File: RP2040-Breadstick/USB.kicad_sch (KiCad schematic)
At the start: 5 parts, among them J601 USB_C_Receptacle_USB2.0

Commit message: More BOM updates
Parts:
- J601: value USB_C_Receptacle_USB2.0 -> (none)
- R601, R602: value 5k1 0603 -> (none); Digikey P123051DKR-ND -> 311-5.10KHRCT-ND; Manufacturer (none) -> YAGEO; Manufacturer_Part_Number (none) -> RC0603FR-075K1L; Mouser (none) -> 603-RC0603FR-075K1L; Package (none) -> 0603
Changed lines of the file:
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@@
       (effects (font (size 1.27 1.27)) (justify left))
     )
-    (property "Value" "5k1 0603" (id 1) (at 128.27 121.92 0)
+    (property "Value" "" (id 1) (at 128.27 121.92 0)
       (effects (font (size 1.27 1.27)) (justify left))
     )
@@
       (effects (font (size 1.27 1.27)) hide)
     )
-    (property "Digikey" "P123051DKR-ND" (id 5) (at 116.84 120.65 0)
+    (property "Digikey" "311-5.10KHRCT-ND" (id 5) (at 116.84 120.65 0)
+      (effects (font (size 1.27 1.27)) hide)
+    )
+    (property "Manufacturer" "YAGEO" (id 6) (at 116.84 120.65 0)
+      (effects (font (size 1.27 1.27)) hide)
+    )
+    (property "Manufacturer_Part_Number" "RC0603FR-075K1L" (id 7) (at 116.84 120.65 0)
+      (effects (font (size 1.27 1.27)) hide)
+    )
+    (property "Mouser" "603-RC0603FR-075K1L" (id 8) (at 116.84 120.65 0)
+      (effects (font (size 1.27 1.27)) hide)
+    )
+    (property "Package" "0603" (id 9) (at 116.84 120.65 0)
       (effects (font (size 1.27 1.27)) hide)
     )
@@
       (effects (font (size 1.27 1.27)) (justify left))
     )
-    (property "Value" "5k1 0603" (id 1) (at 142.24 121.92 0)
+    (property "Value" "" (id 1) (at 142.24 121.92 0)
       (effects (font (size 1.27 1.27)) (justify left))
     )
@@
       (effects (font (size 1.27 1.27)) hide)
     )
-    (property "Digikey" "P123051DKR-ND" (id 5) (at 130.81 120.65 0)
+    (property "Digikey" "311-5.10KHRCT-ND" (id 5) (at 130.81 120.65 0)
+      (effects (font (size 1.27 1.27)) hide)
+    )
+    (property "Manufacturer" "YAGEO" (id 6) (at 130.81 120.65 0)
+      (effects (font (size 1.27 1.27)) hide)
+    )
+    (property "Manufacturer_Part_Number" "RC0603FR-075K1L" (id 7) (at 130.81 120.65 0)
+      (effects (font (size 1.27 1.27)) hide)
+    )
+    (property "Mouser" "603-RC0603FR-075K1L" (id 8) (at 130.81 120.65 0)
+      (effects (font (size 1.27 1.27)) hide)
+    )
+    (property "Package" "0603" (id 9) (at 130.81 120.65 0)
       (effects (font (size 1.27 1.27)) hide)
     )
@@
     (in_bom yes) (on_board yes) (fields_autoplaced)
     (property "Reference" "J601" (id 0) (at 88.9 77.47 0))
-    (property "Value" "USB_C_Receptacle_USB2.0" (id 1) (at 88.9 80.01 0))
+    (property "Value" "" (id 1) (at 88.9 80.01 0))
     (property "Footprint" "" (id 2) (at 92.71 100.33 0)
       (effects (font (size 1.27 1.27)) hide)

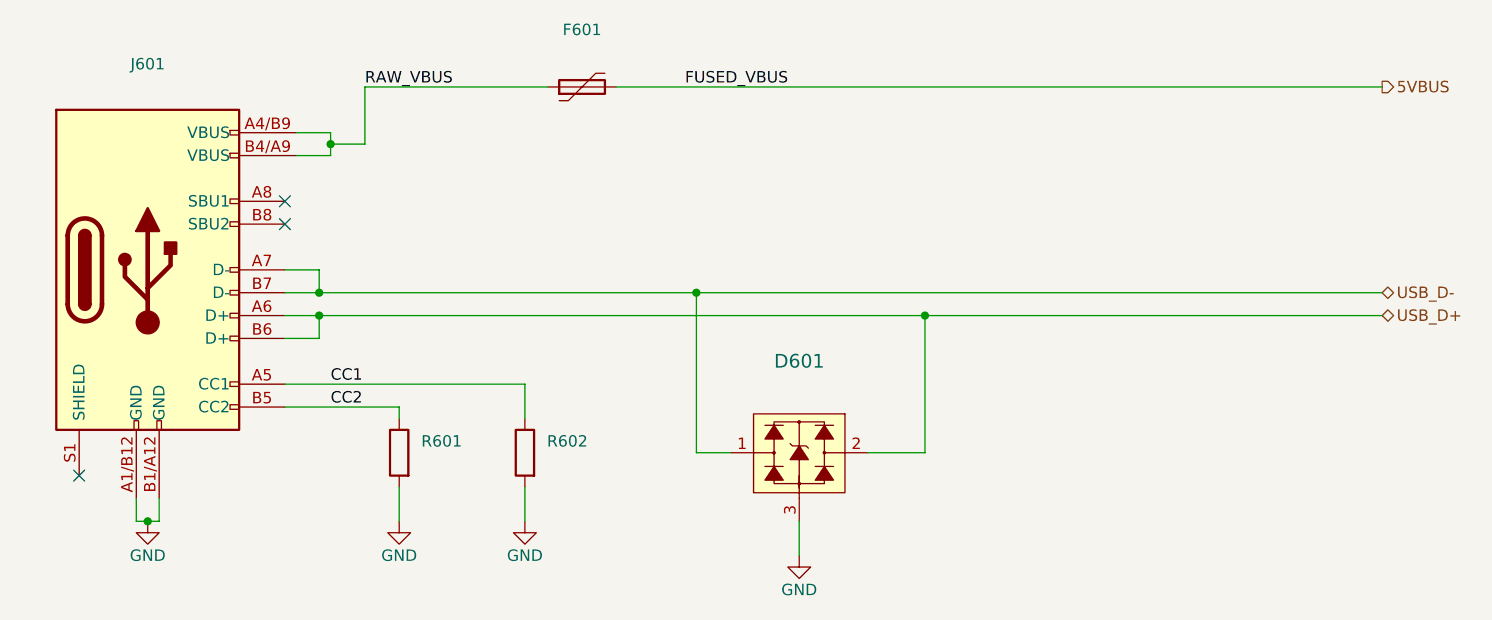
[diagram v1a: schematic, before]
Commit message: Created BOM spreadsheet
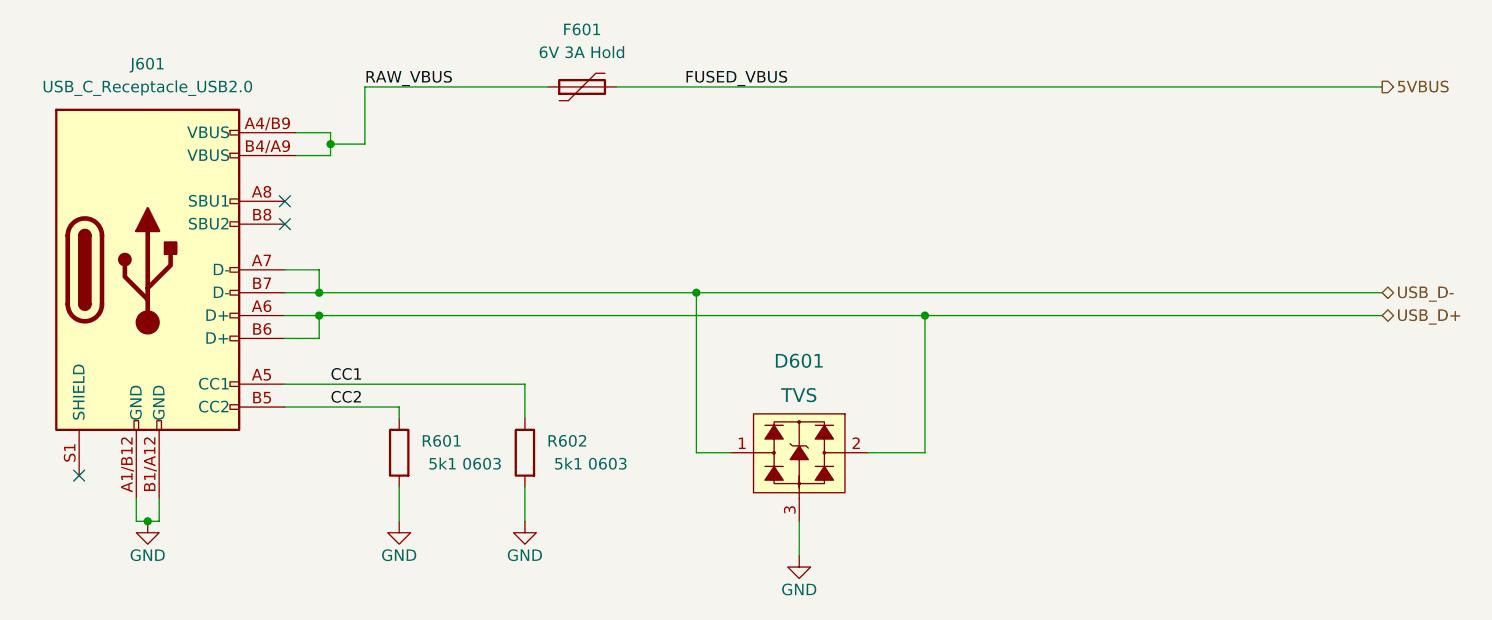
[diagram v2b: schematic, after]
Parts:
- D601: value (none) -> TVS; footprint (none) -> Package_TO_SOT_SMD:SOT-23
- F601: value (none) -> 6V 3A Hold; footprint (none) -> Fuse:Fuse_1206_3216Metric
- J601: value (none) -> USB_C_Receptacle_USB2.0
- R601, R602: value (none) -> 5k1 0603; footprint (none) -> Resistor_SMD:R_0603_1608Metric
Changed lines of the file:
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@@
       (effects (font (size 1.27 1.27)) (justify left))
     )
-    (property "Value" "" (id 1) (at 128.27 121.92 0)
+    (property "Value" "5k1 0603" (id 1) (at 128.27 121.92 0)
       (effects (font (size 1.27 1.27)) (justify left))
     )
-    (property "Footprint" "" (id 2) (at 118.618 120.65 90)
+    (property "Footprint" "Resistor_SMD:R_0603_1608Metric" (id 2) (at 118.618 120.65 90)
       (effects (font (size 1.27 1.27)) hide)
     )
@@
     (in_bom yes) (on_board yes) (fields_autoplaced)
     (property "Reference" "F601" (id 0) (at 137.16 73.66 90))
-    (property "Value" "" (id 1) (at 137.16 76.2 90))
-    (property "Footprint" "" (id 2) (at 142.24 78.74 0)
+    (property "Value" "6V 3A Hold" (id 1) (at 137.16 76.2 90))
+    (property "Footprint" "Fuse:Fuse_1206_3216Metric" (id 2) (at 142.24 78.74 0)
       (effects (font (size 1.27 1.27)) (justify left) hide)
     )
@@
       (effects (font (size 1.524 1.524)))
     )
-    (property "Value" "" (id 1) (at 161.29 114.3 0)
+    (property "Value" "TVS" (id 1) (at 161.29 114.3 0)
       (effects (font (size 1.524 1.524)))
     )
-    (property "Footprint" "" (id 2) (at 156.21 115.57 0)
+    (property "Footprint" "Package_TO_SOT_SMD:SOT-23" (id 2) (at 156.21 115.57 0)
       (effects (font (size 1.524 1.524)) (justify left) hide)
     )
@@
       (effects (font (size 1.27 1.27)) (justify left))
     )
-    (property "Value" "" (id 1) (at 142.24 121.92 0)
+    (property "Value" "5k1 0603" (id 1) (at 142.24 121.92 0)
       (effects (font (size 1.27 1.27)) (justify left))
     )
-    (property "Footprint" "" (id 2) (at 132.588 120.65 90)
+    (property "Footprint" "Resistor_SMD:R_0603_1608Metric" (id 2) (at 132.588 120.65 90)
       (effects (font (size 1.27 1.27)) hide)
     )
@@
     (in_bom yes) (on_board yes) (fields_autoplaced)
     (property "Reference" "J601" (id 0) (at 88.9 77.47 0))
-    (property "Value" "" (id 1) (at 88.9 80.01 0))
+    (property "Value" "USB_C_Receptacle_USB2.0" (id 1) (at 88.9 80.01 0))
     (property "Footprint" "" (id 2) (at 92.71 100.33 0)
       (effects (font (size 1.27 1.27)) hide)

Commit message: Updated crystal caps part numbers in BOM from 0201 to 0603
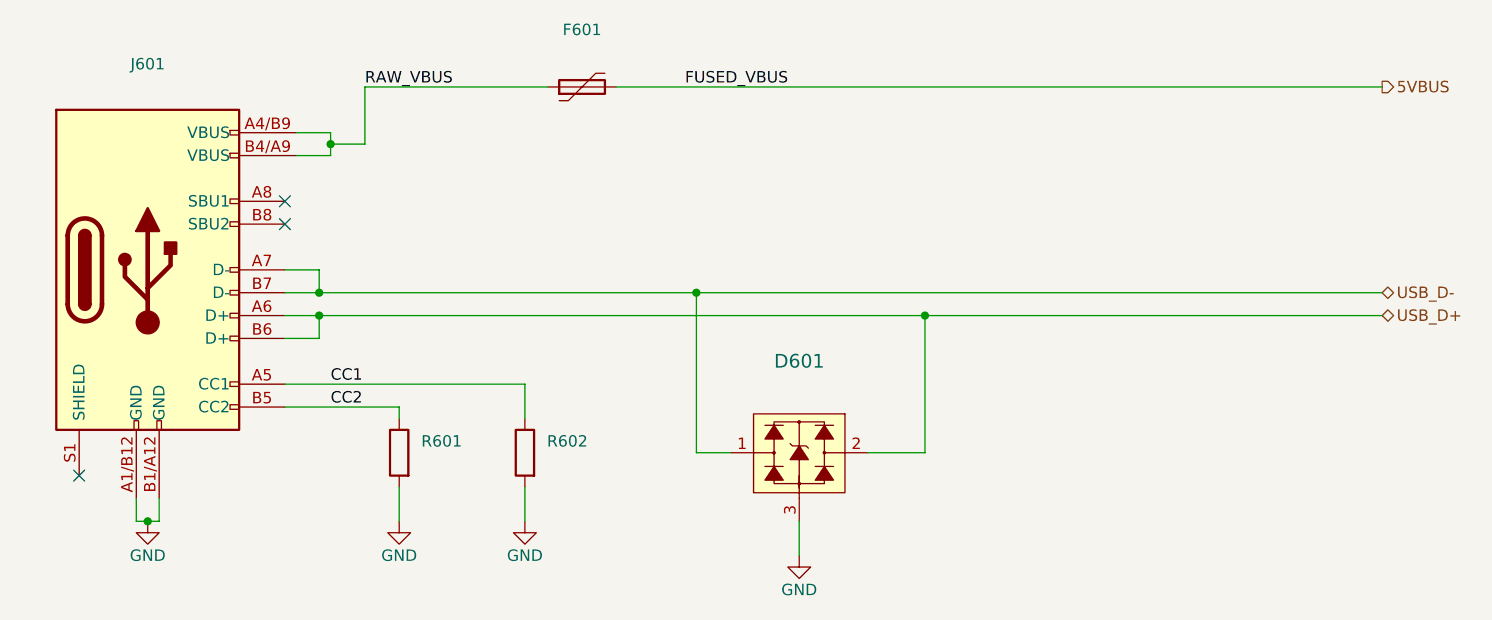
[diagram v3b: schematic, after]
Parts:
- D601: value TVS -> (none); footprint Package_TO_SOT_SMD:SOT-23 -> (none)
- F601: value 6V 3A Hold -> (none); footprint Fuse:Fuse_1206_3216Metric -> (none)
- J601: value USB_C_Receptacle_USB2.0 -> (none)
- R601, R602: value 5k1 0603 -> (none); footprint Resistor_SMD:R_0603_1608Metric -> (none)
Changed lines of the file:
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@@
       (effects (font (size 1.27 1.27)) (justify left))
     )
-    (property "Value" "5k1 0603" (id 1) (at 128.27 121.92 0)
+    (property "Value" "" (id 1) (at 128.27 121.92 0)
       (effects (font (size 1.27 1.27)) (justify left))
     )
-    (property "Footprint" "Resistor_SMD:R_0603_1608Metric" (id 2) (at 118.618 120.65 90)
+    (property "Footprint" "" (id 2) (at 118.618 120.65 90)
       (effects (font (size 1.27 1.27)) hide)
     )
@@
     (in_bom yes) (on_board yes) (fields_autoplaced)
     (property "Reference" "F601" (id 0) (at 137.16 73.66 90))
-    (property "Value" "6V 3A Hold" (id 1) (at 137.16 76.2 90))
-    (property "Footprint" "Fuse:Fuse_1206_3216Metric" (id 2) (at 142.24 78.74 0)
+    (property "Value" "" (id 1) (at 137.16 76.2 90))
+    (property "Footprint" "" (id 2) (at 142.24 78.74 0)
       (effects (font (size 1.27 1.27)) (justify left) hide)
     )
@@
       (effects (font (size 1.524 1.524)))
     )
-    (property "Value" "TVS" (id 1) (at 161.29 114.3 0)
+    (property "Value" "" (id 1) (at 161.29 114.3 0)
       (effects (font (size 1.524 1.524)))
     )
-    (property "Footprint" "Package_TO_SOT_SMD:SOT-23" (id 2) (at 156.21 115.57 0)
+    (property "Footprint" "" (id 2) (at 156.21 115.57 0)
       (effects (font (size 1.524 1.524)) (justify left) hide)
     )
@@
       (effects (font (size 1.27 1.27)) (justify left))
     )
-    (property "Value" "5k1 0603" (id 1) (at 142.24 121.92 0)
+    (property "Value" "" (id 1) (at 142.24 121.92 0)
       (effects (font (size 1.27 1.27)) (justify left))
     )
-    (property "Footprint" "Resistor_SMD:R_0603_1608Metric" (id 2) (at 132.588 120.65 90)
+    (property "Footprint" "" (id 2) (at 132.588 120.65 90)
       (effects (font (size 1.27 1.27)) hide)
     )
@@
     (in_bom yes) (on_board yes) (fields_autoplaced)
     (property "Reference" "J601" (id 0) (at 88.9 77.47 0))
-    (property "Value" "USB_C_Receptacle_USB2.0" (id 1) (at 88.9 80.01 0))
+    (property "Value" "" (id 1) (at 88.9 80.01 0))
     (property "Footprint" "" (id 2) (at 92.71 100.33 0)
       (effects (font (size 1.27 1.27)) hide)

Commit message: Swapped Tantalum Caps for MLCC, added CE, UKCA, RoHS symbols
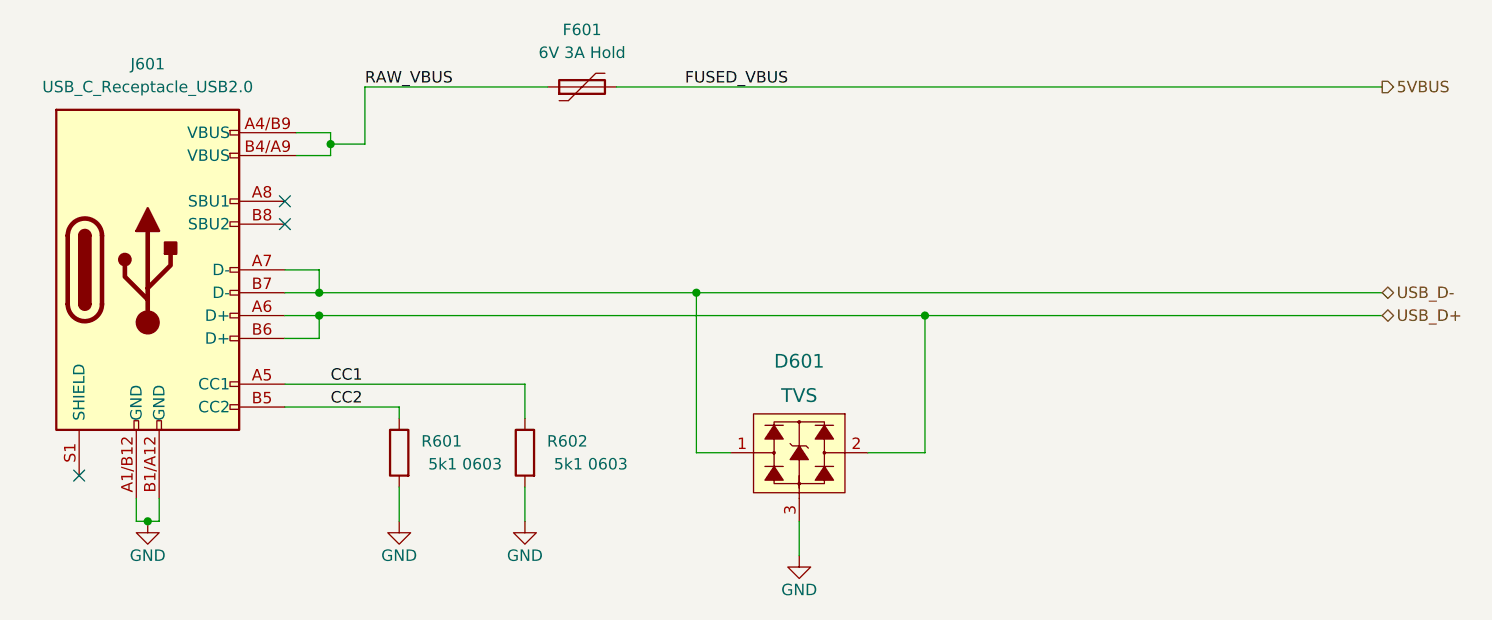
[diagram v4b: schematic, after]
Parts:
- D601: value (none) -> TVS; footprint (none) -> Package_TO_SOT_SMD:SOT-23
- F601: value (none) -> 6V 3A Hold; footprint (none) -> Fuse:Fuse_1206_3216Metric
- J601: value (none) -> USB_C_Receptacle_USB2.0
- R601, R602: value (none) -> 5k1 0603; footprint (none) -> Resistor_SMD:R_0603_1608Metric
